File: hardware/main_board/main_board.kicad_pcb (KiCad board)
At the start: 4 copper layers, 154 x 50 mm, 179 parts, among them J1 USB_C_Receptacle_USB2.0_16P, J3 BAT1, J4 Conn_02x05_Odd_Even, J5 Conn_02x05_Odd_Even, Q1 MMBT3904, Q10 MMBTA42, Q11 MMBTA92, Q12 MMBTA42, Q13 MMBTA92, Q14 MMBTA42, Q15 MMBTA92, Q17 FDMC4435BZ, Q19 FDS2734, Q2 MMBT3904, Q4 MMBTA92, Q5 MMBTA42, Q6 MMBTA42, Q7 MMBTA92, Q8 MMBTA42, Q9 MMBTA92, U1 MPU-6050, U10 HUSB238_002DD, U11 TPS22810DBVR, U12 TPS2121, U13 74HC238, U14 BQ25601, U15 TPS63802, U16 BQ27441DRZR-G1A, U2 CP2102N-A02-GQFN28, U3 SRV05-4, U4 DFPlayer_mini, U5 ESP32-S3-WROOM1, U6 DS3231MZ, U7 TPS22918DBVR, U8 LM5155, U9 TPS61022

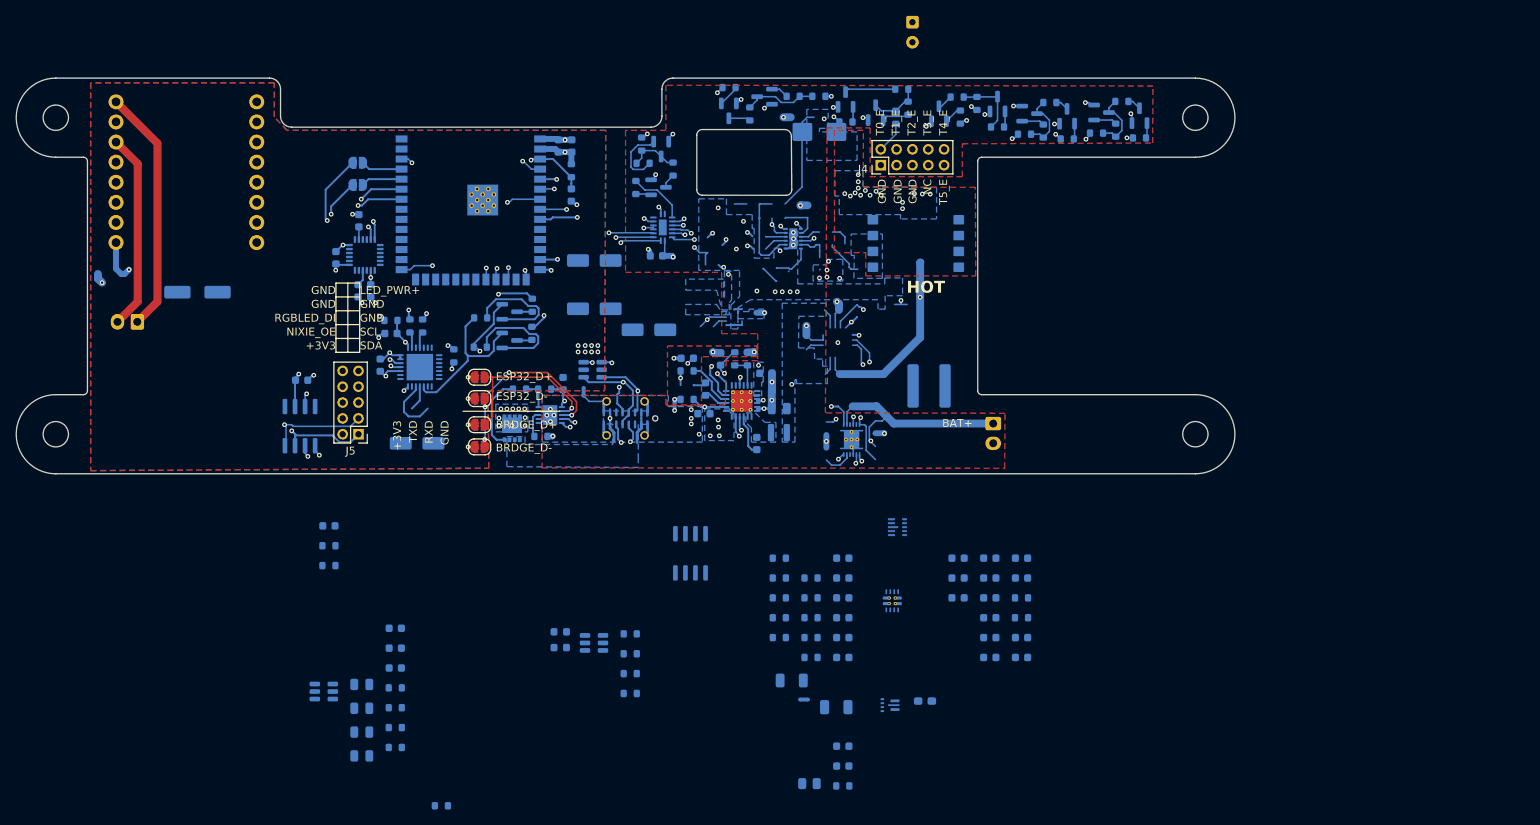
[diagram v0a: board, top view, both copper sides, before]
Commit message: hardware(sch): update component package to 0402 as most as possable, layout is still need to complete
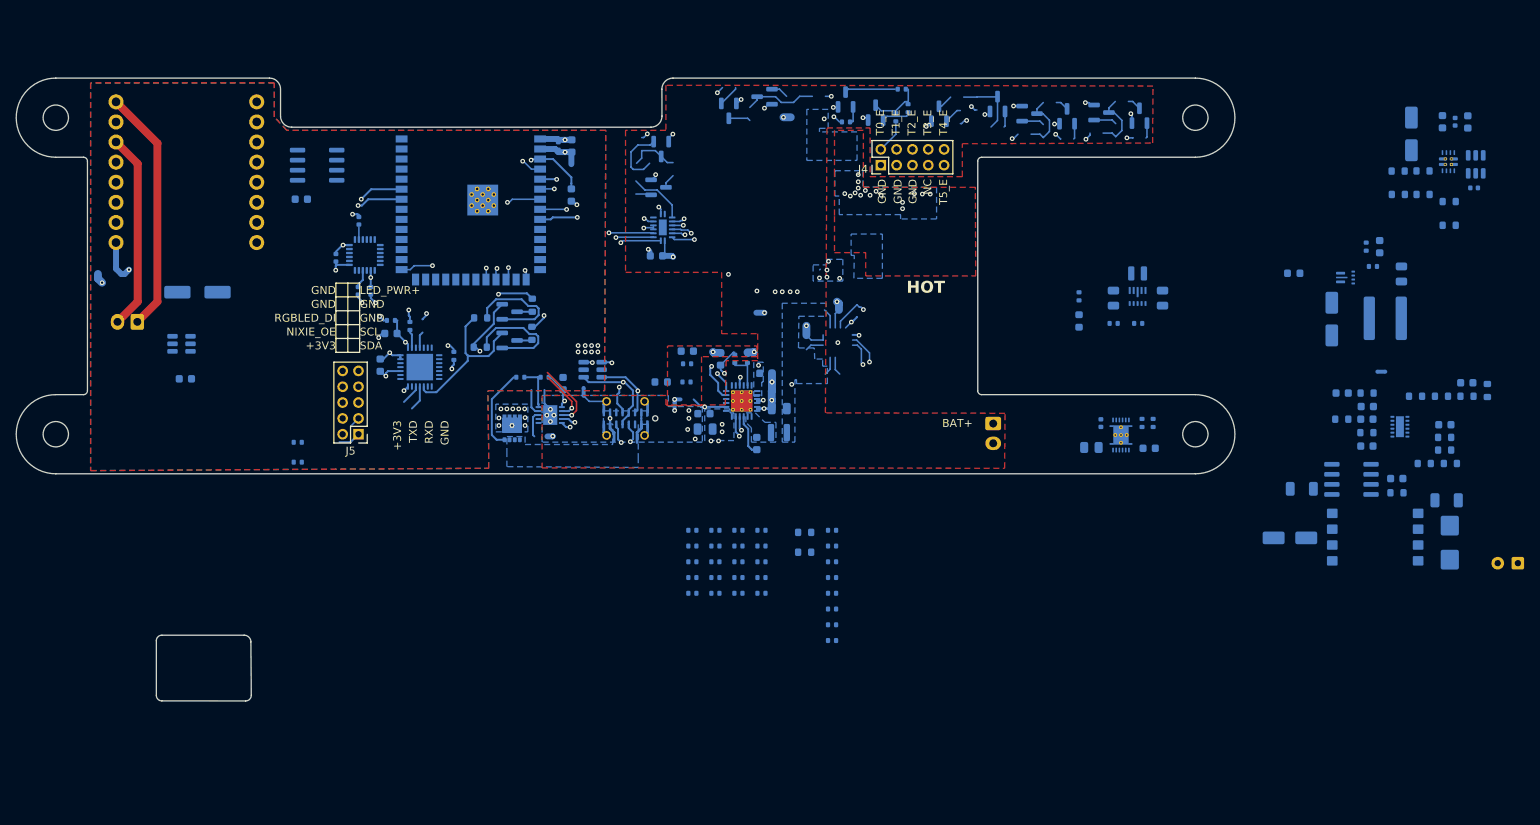
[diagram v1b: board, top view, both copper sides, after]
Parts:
- removed C22: 22u, Capacitor_SMD:C_Elec_5x5.4
- removed JP1, JP2, JP3, JP4: NC, Jumper:SolderJumper-2_P1.3mm_Open_RoundedPad1.0x1.5mm
- removed JP5, JP6: NO, Jumper:SolderJumper-2_P1.3mm_Open_RoundedPad1.0x1.5mm
- removed L5: ER9.5 Transformer, KiCad_Library:Transformer_ER9.5_11.6mmx8.2mm
- removed R53, R58, R62, R85, R87: 10k, Resistor_SMD:R_0603_1608Metric
- removed R54: 470k, Resistor_SMD:R_0603_1608Metric
- removed R55: 1M, Resistor_SMD:R_0603_1608Metric
- removed R56: 47k, Resistor_SMD:R_0603_1608Metric
- removed R60, R67: 10k, Capacitor_SMD:C_0603_1608Metric
- added L2: ER9.5 Transformer, KiCad_Library:Transformer_ER9.5_11.6mmx8.2mm, B.Cu at (240.7, 154.0)
- added R23: 10k, Resistor_SMD:R_0402_1005Metric, B.Cu at (172.1, 161.1)
- added R24: 10k, Resistor_SMD:R_0402_1005Metric, B.Cu at (172.1, 163.1)
- added R25: 10k, Resistor_SMD:R_0402_1005Metric, B.Cu at (172.1, 165.1)
- added R26: 3.3k, Resistor_SMD:R_0402_1005Metric, B.Cu at (172.1, 167.1)
- added R27: 10k, Resistor_SMD:R_0603_1608Metric, B.Cu at (168.6, 153.4)
- added R29: 10k, Resistor_SMD:R_0603_1608Metric, B.Cu at (168.6, 155.9)
- added R30: 10k, Resistor_SMD:R_0402_1005Metric, B.Cu at (163.2, 153.1)
- added R31: 10k, Resistor_SMD:R_0402_1005Metric, B.Cu at (163.2, 155.1)
- added R32: 10k, Resistor_SMD:R_0402_1005Metric, B.Cu at (163.2, 157.1)
- added R33: 10k, Resistor_SMD:R_0402_1005Metric, B.Cu at (163.2, 159.1)
- C12: value 1u -> 100n; footprint Capacitor_SMD:C_0603_1608Metric -> Capacitor_SMD:C_0402_1005Metric
- C15: value 0.47u -> 470n
- C17, C2, C26, C30, C4, C5, C6: footprint Capacitor_SMD:C_0603_1608Metric -> Capacitor_SMD:C_0402_1005Metric
- C24: footprint Capacitor_SMD:C_0603_1608Metric_Pad1.08x0.95mm_HandSolder -> Capacitor_SMD:C_0603_1608Metric
- L3: footprint Capacitor_SMD:C_0603_1608Metric -> habonroof_kicad_library:Murata_201612E
- R1, R10, R11, R12, R15, R16, R17, R18, R19, R2, R21, R28, R34, R35, R36, R38, R39, R4, R40, R42, R43, R44, R47, R48, R5, R52, R57, R6, R63, R64, R66, R86, R9: footprint Resistor_SMD:R_0603_1608Metric -> Resistor_SMD:R_0402_1005Metric
- R37, R41, R45: value 10k -> 470k; footprint Resistor_SMD:R_0603_1608Metric -> Resistor_SMD:R_0402_1005Metric
- R46: value 470k -> 10k; footprint Resistor_SMD:R_0603_1608Metric -> Resistor_SMD:R_0402_1005Metric
- R49: value 10k -> 1M; footprint Resistor_SMD:R_0603_1608Metric -> Resistor_SMD:R_0402_1005Metric
- R50: value 470k -> 1M; footprint Resistor_SMD:R_0603_1608Metric -> Resistor_SMD:R_0402_1005Metric
- R51: value 1M -> 47k; footprint Resistor_SMD:R_0603_1608Metric -> Resistor_SMD:R_0402_1005Metric
- R59, R61, R65, R68, R69, R70: footprint Capacitor_SMD:C_0603_1608Metric -> Resistor_SMD:R_0603_1608Metric
- R72, R73: footprint Capacitor_SMD:C_0603_1608Metric -> Resistor_SMD:R_0402_1005Metric
- R81: value WSLP1206R0330FEA -> SMF12M1FR047T
- moved U11 160.1 mm to (253.4, 106.9), turned to -90 degrees
- moved C29 149.9 mm to (252.4, 101.5), turned to 90 degrees
- moved C30 148.2 mm to (253.2, 109.9), turned to 0 degrees
- moved C9 142.4 mm to (244.0, 120.8), turned to 90 degrees
- moved R3 138.6 mm to (245.8, 136.2), turned to 0 degrees
- moved Rsnub1 135.3 mm to (243.5, 148.4), turned to 0 degrees
- moved Csnub1 135.1 mm to (243.4, 146.6)
- moved C10 131.6 mm to (245.3, 103.0), turned to 90 degrees
- moved C7 112.3 mm to (213.8, 123.8), turned to -90 degrees
- moved C27 111.2 mm to (207.7, 123.8), turned to -90 degrees
- moved D3 104.1 mm to (230.4, 120.7), turned to 0 degrees
- moved R19 100.9 mm to (211.3, 139.6), turned to -90 degrees
- moved C25 100.8 mm to (257.5, 157.3), turned to 180 degrees
- moved D1 95.1 mm to (250.2, 154.7), turned to -90 degrees
- moved R84 94.8 mm to (254.9, 135.5), turned to 90 degrees
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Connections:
- R10 pad 1: +3V3 -> I2C0_SDA
- R10 pad 2: I2C0_SDA -> +3V3
- R37 pad 1: T1_B -> Net-(Q6-C)
- R37 pad 2: Net-(Q6-B) -> Net-(Q7-C)
- R38 pad 1: Net-(Q6-C) -> Net-(Q8-C)
- R38 pad 2: Net-(Q7-C) -> Net-(Q9-C)
- R41 pad 1: T2_B -> Net-(Q14-C)
- R41 pad 2: Net-(Q8-B) -> Net-(Q15-C)
- R42 pad 1: Net-(Q8-C) -> Net-(Q12-C)
- R42 pad 2: Net-(Q9-C) -> Net-(Q13-C)
- R45 pad 1: T3_B -> Net-(Q10-C)
- R45 pad 2: Net-(Q10-B) -> Net-(Q11-C)
- R46 pad 1: Net-(Q10-C) -> T1_B
- R46 pad 2: Net-(Q11-C) -> Net-(Q6-B)
- R47 pad 1: Net-(Q11-B) -> Net-(Q15-B)
- R47 pad 2: Net-(Q11-C) -> Net-(Q15-C)
- R48 pad 1: Net-(Q11-C) -> Net-(Q15-C)
- R48 pad 2: /nixie_anode_mux/T3_E -> /nixie_anode_mux/T5_E
- R49 pad 1: T4_B -> Net-(Q13-B)
- R49 pad 2: Net-(Q12-B) -> Net-(Q13-C)
- R50 pad 1: Net-(Q12-C) -> Net-(Q11-B)
- R50 pad 2: Net-(Q13-C) -> Net-(Q11-C)
- R51 pad 1: Net-(Q13-B) -> Net-(Q13-C)
- R51 pad 2: Net-(Q13-C) -> /nixie_anode_mux/T4_E
- R52 pad 1: Net-(Q13-C) -> Net-(Q11-C)
- R52 pad 2: /nixie_anode_mux/T4_E -> /nixie_anode_mux/T3_E
- U12 pad 8: unconnected-(U12-OUT-Pad8) -> Net-(U11-VIN)
- U2 pad 25: Net-(JP4-A) -> U0TXD
- U2 pad 26: Net-(JP3-A) -> U0RXD
- U2 pad 4: Net-(JP2-B) -> USB_D+
- U2 pad 5: Net-(JP1-B) -> USB_D-
- U5 pad 13: Net-(JP5-B) -> unconnected-(U5-IO19-Pad13)
- U5 pad 14: Net-(JP6-B) -> unconnected-(U5-IO20-Pad14)
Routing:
- net VBAT: track 102.8 -> 0.00 mm, vias 3 -> 0
- net I2C0_SCL: track 164.4 -> 74.8 mm, vias 6 -> 3
- net I2C0_SDA: track 158.2 -> 72.9 mm, vias 6 -> 3
- net Net-(JP3-A): track 65.3 -> 0.00 mm, vias 1 -> 0
- net Net-(JP4-A): track 60.1 -> 0.00 mm, vias 1 -> 0
- net HV_PWR+: track 48.2 -> 2.35 mm, vias 2 -> 0
- net ~{RTC_INT}: track 41.9 -> 0.00 mm, vias 2 -> 0
- net Net-(U8-UVLO/EN/SYNC): track 34.2 -> 0.00 mm, vias 3 -> 0
- net Net-(JP5-B): track 25.9 -> 0.00 mm, vias 2 -> 0
- net Net-(JP6-B): track 21.8 -> 0.00 mm, vias 2 -> 0
- net Net-(JP1-B): track 21.4 -> 0.00 mm, vias 2 -> 0
- net +3V3: track 153.0 -> 132.7 mm, vias 9 -> 7
- net Net-(JP2-B): track 17.8 -> 0.00 mm, vias 2 -> 0
- net USB_D-: track 53.0 -> 36.4 mm, vias 7 -> 4
- net DF_EN: track 36.5 -> 21.3 mm, vias 2 -> 1
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- removed copper zone on B.Cu, net +3V3
- removed copper zone on B.Cu, net +5V
- removed copper zone on B.Cu, net Net-(U9-SW)
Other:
- board size 154 x 50 mm -> 154 x 78.7 mm
- board text removed: "BRDGE_D+"
- board text removed: "BRDGE_D-"
- board text removed: "ESP32_D+"
- board text removed: "ESP32_D-"

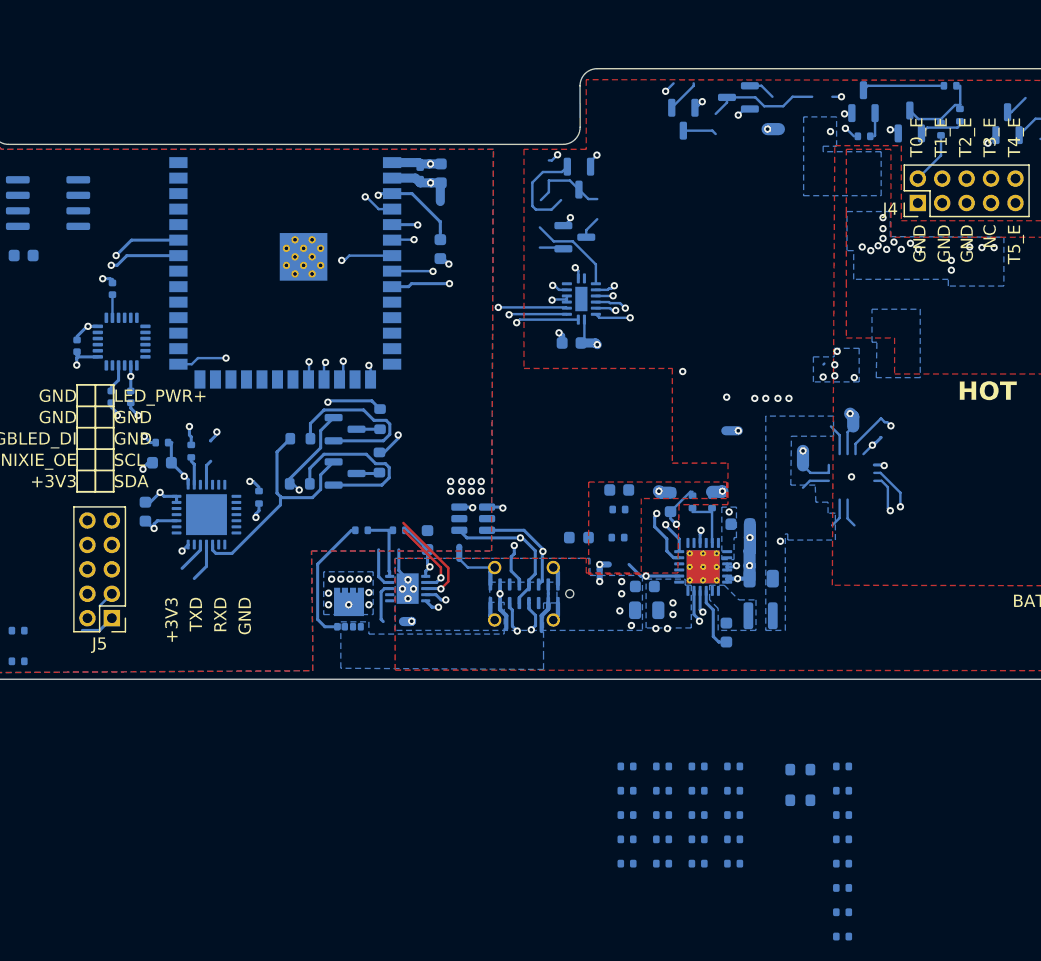
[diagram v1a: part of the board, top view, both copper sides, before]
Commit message: hardware(als): Add ALS sensor LTR-303ALS to detect light, add push button as input.
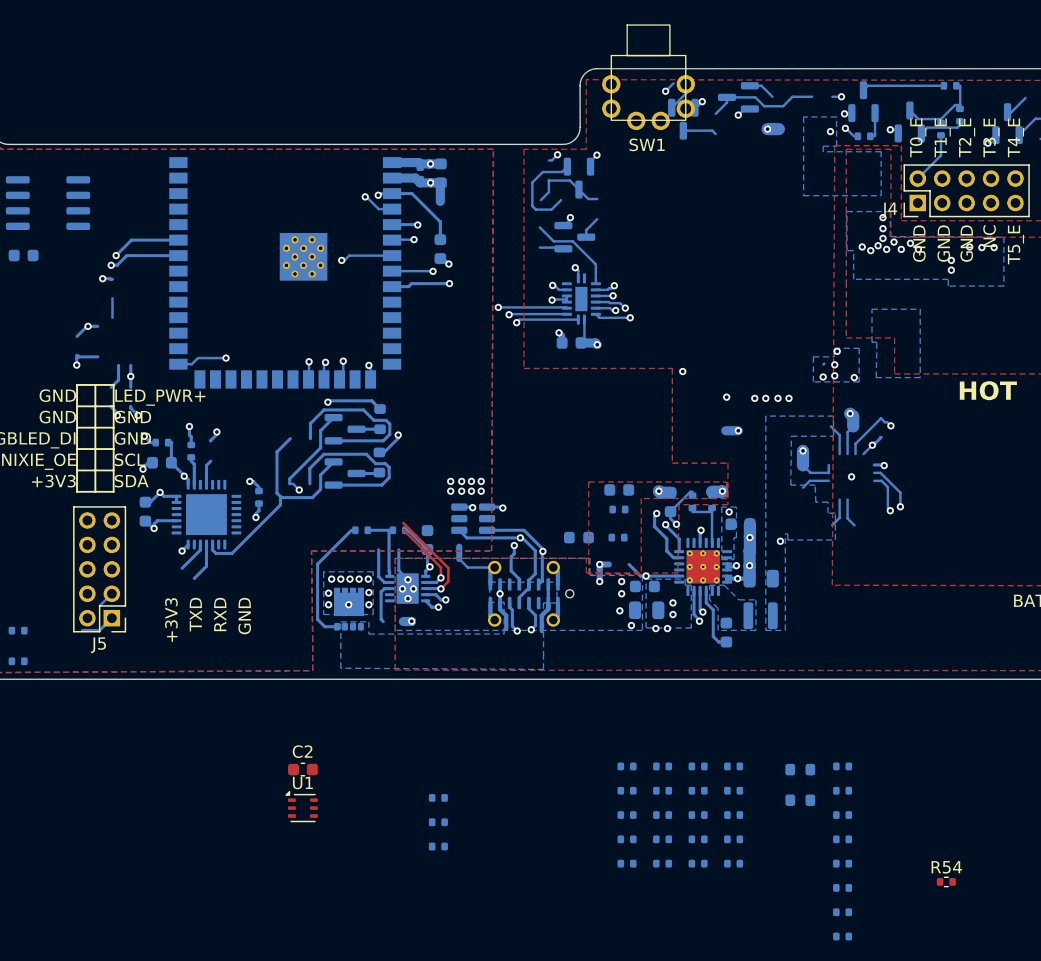
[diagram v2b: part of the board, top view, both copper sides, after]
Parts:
- removed C4, C5: 100n, Capacitor_SMD:C_0402_1005Metric
- removed C6: 2.2n, Capacitor_SMD:C_0402_1005Metric
- added R53: 10k, Resistor_SMD:R_0402_1005Metric, B.Cu at (139.0, 159.7)
- added R54: 10k, Resistor_SMD:R_0402_1005Metric, F.Cu at (180.6, 162.6)
- added SW1: XKB5858-W-E-75, habonroof_kicad_library:XKB5858, F.Cu at (156.2, 97.6)
- C2: value 10n -> 1u; footprint Capacitor_SMD:C_0402_1005Metric -> Capacitor_SMD:C_0603_1608Metric; moved to F.Cu
- R7, R8: footprint Resistor_SMD:R_0603_1608Metric -> Resistor_SMD:R_0402_1005Metric
- U1: value MPU-6050 -> LTR-303ALS-01; footprint Sensor_Motion:InvenSense_QFN-24_4x4mm_P0.5mm -> OptoDevice:Lite-On_LTR-303ALS-01; moved to F.Cu
- moved U1 41.0 mm to (127.9, 156.6), turned to 0 degrees
- moved C2 39.3 mm to (127.9, 153.4), turned to 0 degrees
- moved R7 31.5 mm to (139.0, 155.7)
- moved R8 29.9 mm to (139.0, 157.7)
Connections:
- C2 pad 1: GND -> +3V3
- C2 pad 2: +3V3 -> GND
- R1 pad 2: VSYS -> +5V
- U1 pad 1: unconnected-(U1-CLKIN-Pad1) -> +3V3
- U1 pad 3: unconnected-(U1-NC-Pad3) -> GND
- U1 pad 4: unconnected-(U1-NC-Pad4) -> I2C1_SCL
- U1 pad 6: unconnected-(U1-AUX_DA-Pad6) -> I2C1_SDA
- U5 pad 12: unconnected-(U5-IO8-Pad12) -> BTN_0
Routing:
- net (no net): track 5.68 -> 9.33 mm
- net Net-(U1-REGOUT): track 2.05 -> 0.00 mm
- net Net-(U1-CPOUT): track 1.60 -> 0.00 mm
